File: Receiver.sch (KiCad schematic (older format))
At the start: 25 parts, among them U1 TL074

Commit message: Add files via upload
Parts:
- removed 1M1: R, Resistors_SMD:R_0603, symbol R
- added R?: 1K, Resistors_SMD:R_0603, symbol device:R
- C1, C3, C4, C5, C6, C7, C8: symbol C_Small -> device:C_Small
- C2: symbol CP1_Small -> device:CP1_Small
- D1: symbol BPW34 -> Receiver-rescue:BPW34-opto
- D2: symbol D -> device:D
- R1, R10, R11, R2, R3, R4, R5, R6, R7, R8, R9: symbol R -> device:R
- RV1, RV2: symbol POT -> Receiver-rescue:POT-device
- U1: symbol TL074 -> Receiver-rescue:TL074-linear
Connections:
- wire segments 65 -> 84
- no-connect marks 0 -> 2

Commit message: Add files via upload
Netzliste erstellt und Anfang von Layout
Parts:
- removed C2: CP1_Small, symbol device:CP1_Small
- added C2: 1u 50V, Capacitor_SMD:C_0603_1608Metric, symbol device:C_Small
- C1, C3, C4, C5, C6, C7, C8: footprint Capacitors_SMD:C_0603 -> Capacitor_SMD:C_0603_1608Metric
- D1: footprint Opto-Devices:PhotoDiode_DIL2_4.3x4.65_RM5.08 -> OptoDevice:Osram_DIL2_4.3x4.65mm_P5.08mm
- R1, R10, R2, R3, R4, R5, R6, R7, R8, R9: footprint Resistors_SMD:R_0603 -> Resistor_SMD:R_0603_1608Metric
- R11: renamed from R?; footprint Resistors_SMD:R_0603 -> Resistor_SMD:R_0603_1608Metric
- R12: renamed from R11; footprint Resistors_SMD:R_0603 -> Resistor_SMD:R_0603_1608Metric
- RV1, RV2: footprint (none) -> SparkFun-Electromechanical:TRIM_POT
- U1: value TL074 -> TL074 (ggf. durch TLV4172IPWR ersetzen); footprint Housings_SSOP:TSSOP-14_4.4x5mm_Pitch0.65mm -> Package_SO:TSSOP-14_4.4x5mm_P0.65mm

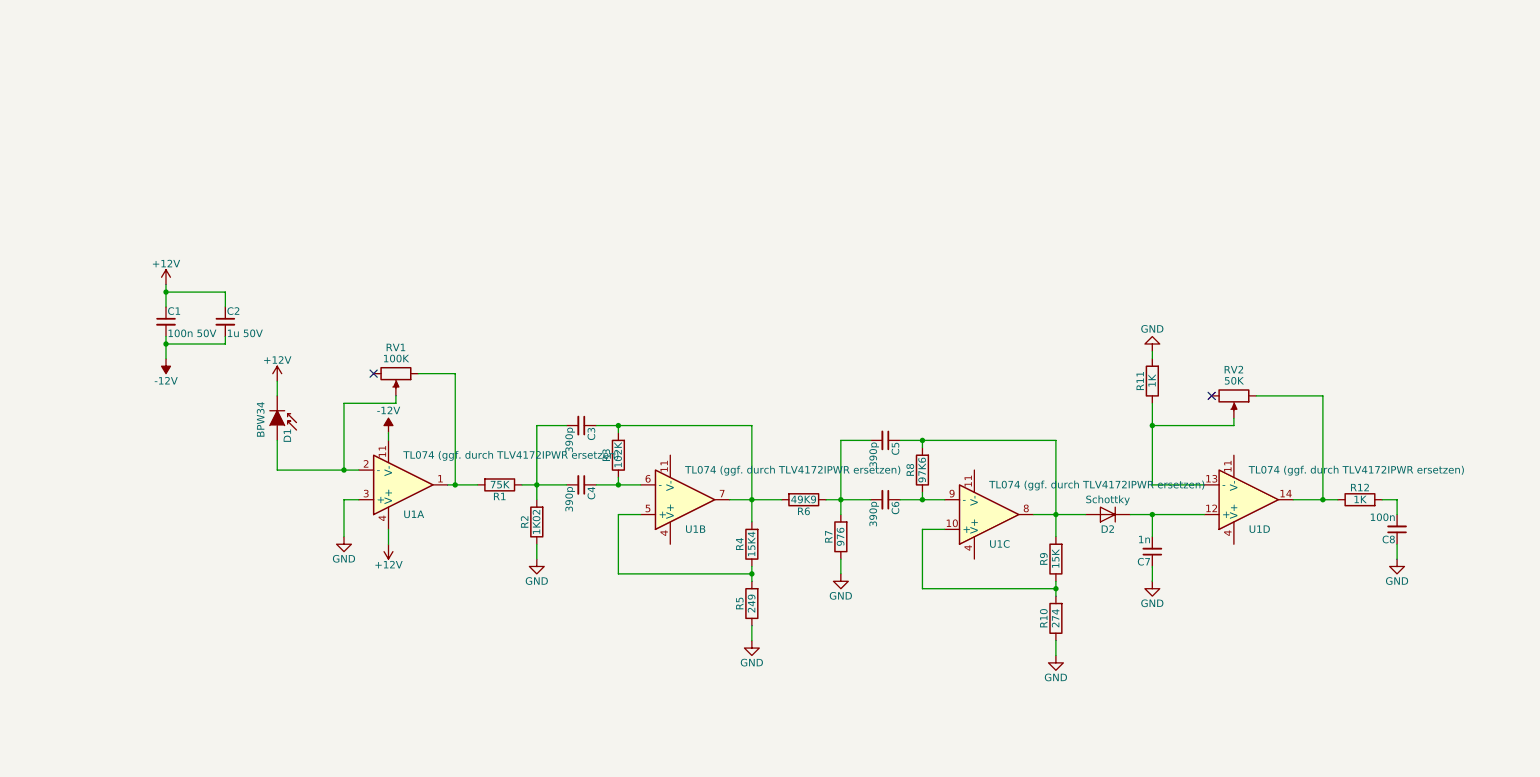
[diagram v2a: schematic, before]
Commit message: Add MST 201 banana plug to the library
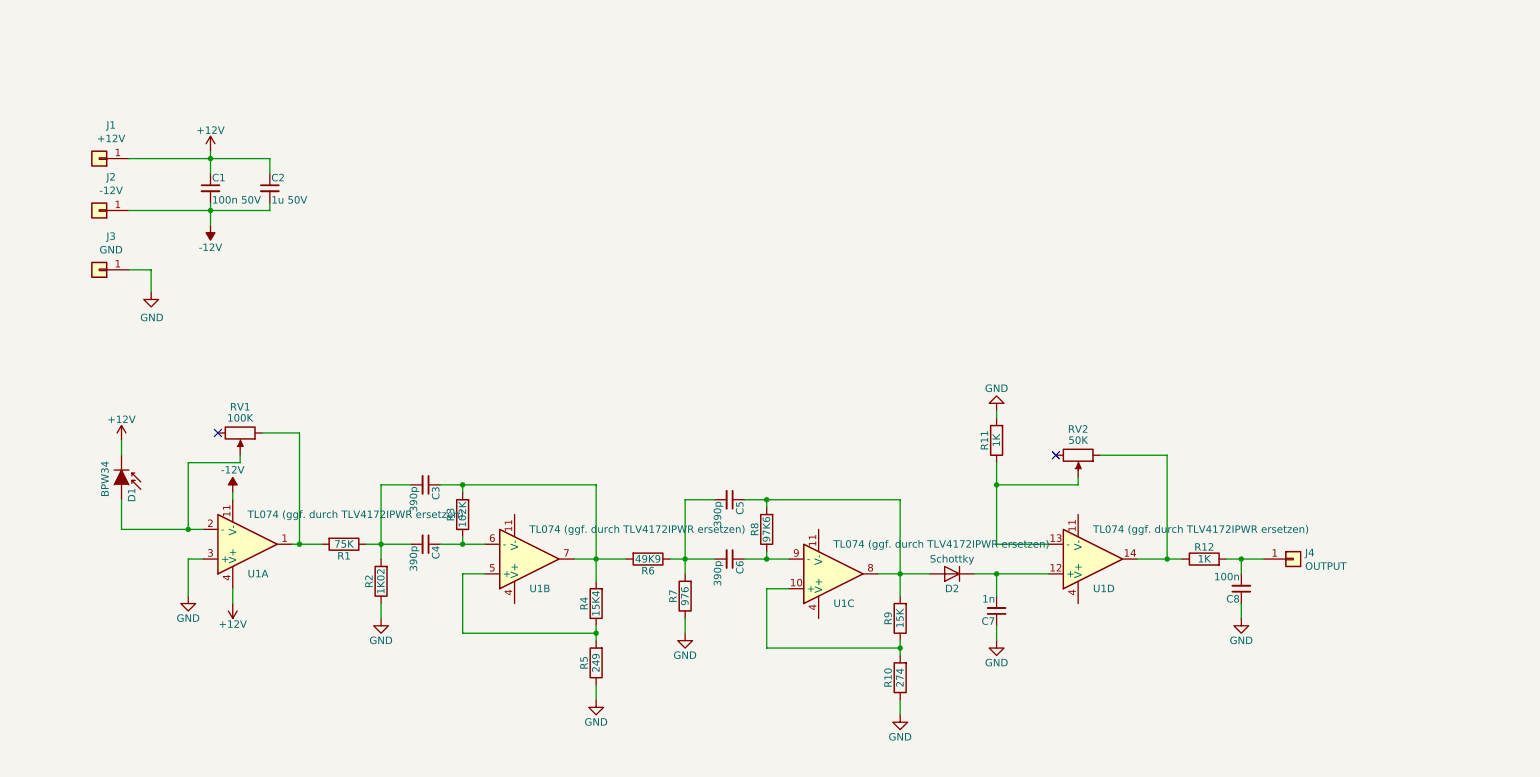
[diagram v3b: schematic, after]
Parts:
- added J1: +12V, optoreceiver:Hirschmann_MST201, symbol Connector:Conn_01x01
- added J2: -12V, optoreceiver:Hirschmann_MST201, symbol Connector:Conn_01x01
- added J3: GND, optoreceiver:Hirschmann_MST201, symbol Connector:Conn_01x01
- added J4: OUTPUT, optoreceiver:Hirschmann_MST201, symbol Connector:Conn_01x01
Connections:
- net +12V: now also J1.1 (Pin_1)
- net -12V: now also J2.1 (Pin_1)
- net GND: now also J3.1 (Pin_1)
- net at C8.2, R12.2: now also J4.1 (Pin_1)
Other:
- moved on the sheet: C1, C2, C3, C4, C5, C6, C7, C8, D1, D2, R1, R10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

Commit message: Update schematic and pcb
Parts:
- added D3, D4: LED, LEDs:LED_0603, symbol device:LED
- added J5: Conn_01x04, Pin_Headers:Pin_Header_Straight_1x04_Pitch2.54mm, symbol Connector:Conn_01x04
- added R13, R14: 1k, Resistors_SMD:R_0603, symbol device:R
- D2: value Schottky -> BAT54; footprint Diodes_SMD:D_SOD-123 -> Diodes_SMD:D_SOT-23_ANK
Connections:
- net +12V: now also J5.2 (Pin_2), R13.1
- net -12V: now also J5.3 (Pin_3), R14.1
- net GND: now also D3.1 (K), D4.2 (A), J5.4 (Pin_4)
- net OUTPUT: now reaches C8.2, J4.1 (Pin_1), R12.2
- net OUTPUT: now also J5.1 (Pin_1)
- new net: D3.2 (A), R13.2
- new net: D4.1 (K), R14.2
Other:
- moved on the sheet: J4
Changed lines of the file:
@@
 P 7700 4300
 F 0 "D2" H 7700 4400 50  0000 C CNN
-F 1 "Schottky " H 7700 4200 50  0000 C CNN
-F 2 "Diodes_SMD:D_SOD-123" H 7700 4300 50  0001 C CNN
+F 1 "BAT54" H 7700 4200 50  0000 C CNN
+F 2 "Diodes_SMD:D_SOT-23_ANK" H 7700 4300 50  0001 C CNN
 F 3 "" H 7700 4300 50  0001 C CNN
 	1    7700 4300
@@
 L Connector:Conn_01x01 J4
 U 1 1 5B03236E
-P 10000 4200
-F 0 "J4" H 10080 4242 50  0000 L CNN
-F 1 "OUTPUT" H 10080 4151 50  0000 L CNN
-F 2 "optoreceiver:Hirschmann_MST201" H 10000 4200 50  0001 C CNN
-F 3 "~" H 10000 4200 50  0001 C CNN
-	1    10000 4200
-	1    0    0    -1
+P 1950 1100
+F 0 "J4" H 2030 1142 50  0000 L CNN
+F 1 "OUTPUT" H 2030 1051 50  0000 L CNN
+F 2 "optoreceiver:Hirschmann_MST201" H 1950 1100 50  0001 C CNN
+F 3 "~" H 1950 1100 50  0001 C CNN
+	1    1950 1100
+	-1   0    0    1
 $EndComp
 Wire Wire Line
@@
 Wire Wire Line
 	2300 2250 2300 2400
+$Comp
+L device:LED D3
+U 1 1 5B14466C
+P 4300 2050
+F 0 "D3" V 4338 1933 50  0000 R CNN
+F 1 "LED" V 4247 1933 50  0000 R CNN
+F 2 "LEDs:LED_0603" H 4300 2050 50  0001 C CNN
+F 3 "~" H 4300 2050 50  0001 C CNN
+	1    4300 2050
+	0    -1   -1   0
+$EndComp
+Wire Wire Line
+	4300 2200 4300 2250
+$Comp
+L device:R R13
+U 1 1 5B14B3A1
+P 3700 1500
+F 0 "R13" H 3770 1546 50  0000 L CNN
+F 1 "1k" H 3770 1455 50  0000 L CNN
+F 2 "Resistors_SMD:R_0603" V 3630 1500 50  0001 C CNN
+F 3 "" H 3700 1500 50  0001 C CNN
+	1    3700 1500
+	0    -1   -1   0
+$EndComp
+$Comp
+L Connector:Conn_01x04 J5
+U 1 1 5B150E6D
+P 4850 1750
+F 0 "J5" H 4770 2067 50  0000 C CNN
+F 1 "Conn_01x04" H 4770 1976 50  0000 C CNN
+F 2 "Pin_Headers:Pin_Header_Straight_1x04_Pitch2.54mm" H 4850 1750 50  0001 C CNN
+F 3 "~" H 4850 1750 50  0001 C CNN
+	1    4850 1750
+	-1   0    0    -1
+$EndComp
+Text Label 2250 1100 0    50   ~ 0
+OUTPUT
+Wire Wire Line
+	2250 1100 2150 1100
+Text Label 9800 4200 0    50   ~ 0
+OUTPUT
+$Comp
+L power:GND #PWR0101
+U 1 1 5B156865
+P 5100 2000
+F 0 "#PWR0101" H 5100 1750 50  0001 C CNN
+F 1 "GND" H 5105 1827 50  0000 C CNN
+F 2 "" H 5100 2000 50  0001 C CNN
+F 3 "" H 5100 2000 50  0001 C CNN
+	1    5100 2000
+	1    0    0    -1
+$EndComp
+Wire Wire Line
+	5050 1950 5100 1950
+Wire Wire Line
+	5100 1950 5100 2000
+$Comp
+L power:+12V #PWR0102
+U 1 1 5B15914A
+P 5150 1750
+F 0 "#PWR0102" H 5150 1600 50  0001 C CNN
+F 1 "+12V" V 5165 1878 50  0000 L CNN
+F 2 "" H 5150 1750 50  0001 C CNN
+F 3 "" H 5150 1750 50  0001 C CNN
+	1    5150 1750
+	0    1    1    0
+$EndComp
+$Comp
+L power:-12V #PWR15
+U 1 1 5B15948E
+P 5150 1850
+F 0 "#PWR15" H 5150 1950 50  0001 C CNN
+F 1 "-12V" V 5165 1978 50  0000 L CNN
+F 2 "" H 5150 1850 50  0001 C CNN
+F 3 "" H 5150 1850 50  0001 C CNN
+	1    5150 1850
+	0    1    1    0
+$EndComp
+Wire Wire Line
+	5150 1850 5050 1850
+Wire Wire Line
+	5150 1750 5050 1750
+Text Label 5150 1650 0    50   ~ 0
+OUTPUT
+Wire Wire Line
+	5150 1650 5050 1650
+Wire Wire Line
+	3100 1500 3550 1500
+Connection ~ 3100 1500
+Wire Wire Line
+	2300 2250 4100 2250
+Connection ~ 2300 2250
+$Comp
+L device:R R14
+U 1 1 5B17749B
+P 3700 1850
+F 0 "R14" H 3770 1896 50  0000 L CNN
+F 1 "1k" H 3770 1805 50  0000 L CNN
+F 2 "Resistors_SMD:R_0603" V 3630 1850 50  0001 C CNN
+F 3 "" H 3700 1850 50  0001 C CNN
+	1    3700 1850
+	0    -1   -1   0
+$EndComp
+Wire Wire Line
+	3550 1850 3100 1850
+Connection ~ 3100 1850
+$Comp
+L device:LED D4
+U 1 1 5B182712
+P 4100 2050
+F 0 "D4" V 4138 1933 50  0000 R CNN
+F 1 "LED" V 4047 1933 50  0000 R CNN
+F 2 "LEDs:LED_0603" H 4100 2050 50  0001 C CNN
+F 3 "~" H 4100 2050 50  0001 C CNN
+	1    4100 2050
+	0    1    1    0
+$EndComp
+Wire Wire Line
+	4100 2200 4100 2250
+Connection ~ 4100 2250
+Wire Wire Line
+	4100 2250 4300 2250
+Wire Wire Line
+	3850 1850 4100 1850
+Wire Wire Line
+	4100 1850 4100 1900
+Wire Wire Line
+	3850 1500 4300 1500
+Wire Wire Line
+	4300 1500 4300 1900
 $EndSCHEMATC

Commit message: Add files via upload
- Platzierung und Silkscreen angepasst
- 3D Modelle ergänzt
- aktuelle Renderbilder erzeugt
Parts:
- C1, C2, C3, C4, C5, C6, C7, C8: symbol device:C_Small -> Device:C_Small
- D2: symbol device:D -> Device:D
- D3, D4: symbol device:LED -> Device:LED
- J1, J2, J3, J4: symbol Connector:Conn_01x01 -> Connector:Conn_01x01_Female
- J5: symbol Connector:Conn_01x04 -> Connector:Conn_01x04_Female
- R1, R10, R11, R12, R13, R14, R2, R3, R4, R5, R6, R7, R8, R9: symbol device:R -> Device:R
- RV1, RV2: footprint SparkFun-Electromechanical:TRIM_POT -> User-Submitted:BOURNS-3362P_pot
- U1: footprint Package_SO:TSSOP-14_4.4x5mm_P0.65mm -> Package_SO:SOIC-14_3.9x8.7mm_P1.27mm
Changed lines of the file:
@@
 F 0 "U1" H 2950 4300 50  0000 L CNN
 F 1 "TL074 (ggf. durch TLV4172IPWR ersetzen)" H 2950 3900 50  0000 L CNN
-F 2 "Package_SO:TSSOP-14_4.4x5mm_P0.65mm" H 2900 4200 50  0001 C CNN
+F 2 "Package_SO:SOIC-14_3.9x8.7mm_P1.27mm" H 2900 4200 50  0001 C CNN
 F 3 "" H 3000 4300 50  0001 C CNN
 	1    2950 4100
@@
 $EndComp
 $Comp
-L power:-12V #PWR5
+L power:-12V #PWR05
 U 1 1 5AEAF2F4
 P 2850 3750
-F 0 "#PWR5" H 2850 3850 50  0001 C CNN
+F 0 "#PWR05" H 2850 3850 50  0001 C CNN
 F 1 "-12V" H 2850 3900 50  0000 C CNN
 F 2 "" H 2850 3750 50  0001 C CNN
@@
 	1    0    0    -1
 $EndComp
-Wire Wire Line
-	2850 4400 2850 4500
-Wire Wire Line
-	2850 3750 2850 3800
 Wire Wire Line
 	2550 4000 2650 4000
@@
 F 0 "U1" H 4850 4400 50  0000 L CNN
 F 1 "TL074 (ggf. durch TLV4172IPWR ersetzen)" H 4850 4000 50  0000 L CNN
-F 2 "Package_SO:TSSOP-14_4.4x5mm_P0.65mm" H 4800 4300 50  0001 C CNN
+F 2 "Package_SO:SOIC-14_3.9x8.7mm_P1.27mm" H 4800 4300 50  0001 C CNN
 F 3 "" H 4900 4400 50  0001 C CNN
 	2    4850 4200
@@
 $EndComp
 $Comp
-L device:R R1
+L Device:R R1
 U 1 1 5AEAF541
 P 3600 4100
@@
 $EndComp
 $Comp
-L device:R R2
+L Device:R R2
 U 1 1 5AEAF581
 P 3850 4350
@@
 	3850 3700 3850 4100
 $Comp
-L device:C_Small C4
+L Device:C_Small C4
 U 1 1 5AEAF686
 P 4150 4100
@@
 $EndComp
 $Comp
-L device:C_Small C3
+L Device:C_Small C3
 U 1 1 5AEAF715
 P 4150 3700
@@
 	4250 4100 4400 4100
 $Comp
-L device:R R3
+L Device:R R3
 U 1 1 5AEAF96B
 P 4400 3900
@@
 Connection ~ 4400 3700
 $Comp
-L device:R R4
+L Device:R R4
 U 1 1 5AEAFA8E
 P 5300 4500
@@
 $EndComp
 $Comp
-L device:R R5
+L Device:R R5
 U 1 1 5AEAFAD7
 P 5300 4900
@@
 F 0 "U1" H 6900 4500 50  0000 L CNN
 F 1 "TL074 (ggf. durch TLV4172IPWR ersetzen)" H 6900 4100 50  0000 L CNN
-F 2 "Package_SO:TSSOP-14_4.4x5mm_P0.65mm" H 6850 4400 50  0001 C CNN
+F 2 "Package_SO:SOIC-14_3.9x8.7mm_P1.27mm" H 6850 4400 50  0001 C CNN
 F 3 "" H 6950 4500 50  0001 C CNN
 	3    6900 4300
@@
 $EndComp
 $Comp
-L device:R R6
+L Device:R R6
 U 1 1 5AEAFDA7
 P 5650 4200
@@
 $EndComp
 $Comp
-L device:R R7
+L Device:R R7
 U 1 1 5AEAFDAD
 P 5900 4450
@@
 	5900 3800 5900 4200
 $Comp
-L device:C_Small C6
+L Device:C_Small C6
 U 1 1 5AEAFDBC
 P 6200 4200
@@
 $EndComp
 $Comp
-L device:C_Small C5
+L Device:C_Small C5
 U 1 1 5AEAFDC2
 P 6200 3800
@@
 	6300 4200 6450 4200
 $Comp
-L device:R R8
+L Device:R R8
 U 1 1 5AEAFDC9
 P 6450 4000
@@
 Connection ~ 6450 3800
 $Comp
-L device:R R9
+L Device:R R9
 U 1 1 5AEAFDD8
 P 7350 4600
@@
 $EndComp
 $Comp
-L device:R R10
+L Device:R R10
 U 1 1 5AEAFDDE
 P 7350 5000
@@
 	7350 5150 7350 5250
 $Comp
-L device:C_Small C1
+L Device:C_Small C1
 U 1 1 5AEAFE56
 P 2700 1700
@@
 	2700 1450 2700 1500
 $Comp
-L power:-12V #PWR2
+L power:-12V #PWR02
 U 1 1 5AEAFF86
 P 2700 1950
-F 0 "#PWR2" H 2700 2050 50  0001 C CNN
+F 0 "#PWR02" H 2700 2050 50  0001 C CNN
 F 1 "-12V" H 2700 2100 50  0000 C CNN
 F 2 "" H 2700 1950 50  0001 C CNN
@@
 F 0 "RV2" V 8375 3500 50  0000 C CNN
 F 1 "50K" V 8450 3500 50  0000 C CNN
-F 2 "SparkFun-Electromechanical:TRIM_POT" H 8550 3500 50  0001 C CNN
+F 2 "User-Submitted:BOURNS-3362P_pot" H 8550 3500 50  0001 C CNN
 F 3 "" H 8550 3500 50  0001 C CNN
 	1    8550 3500
@@
 $EndComp
 $Comp
-L device:D D2
+L Device:D D2
 U 1 1 5AEB05C3
 P 7700 4300
@@
 $EndComp
 $Comp
-L device:C_Small C7
+L Device:C_Small C7
 U 1 1 5AEB0668
 P 8000 4550
@@
 Wire Wire Line
 	7850 4300 8000 4300
-$Comp
-L Receiver-rescue:TL074-linear U1
-U 4 1 5AEB085F
-P 8650 4200
-F 0 "U1" H 8650 4400 50  0000 L CNN
-F 1 "TL074 (ggf. durch TLV4172IPWR ersetzen)" H 8650 4000 50  0000 L CNN
-F 2 "Package_SO:TSSOP-14_4.4x5mm_P0.65mm" H 8600 4300 50  0001 C CNN
-F 3 "" H 8700 4400 50  0001 C CNN
-	4    8650 4200
-	1    0    0    1
-$EndComp
 Connection ~ 8000 4300
 Wire Wire Line
@@
 	8950 4200 9150 4200
 $Comp
-L device:R R12
+L Device:R R12
 U 1 1 5AEB0CD1
 P 9400 4200
@@
 Connection ~ 9150 4200
 $Comp
-L device:C_Small C8
+L Device:C_Small C8
 U 1 1 5AEB0DB0
 P 9650 4400
@@
 F 0 "RV1" V 2725 3350 50  0000 C CNN
 F 1 "100K" V 2800 3350 50  0000 C CNN
-F 2 "SparkFun-Electromechanical:TRIM_POT" H 2900 3350 50  0001 C CNN
+F 2 "User-Submitted:BOURNS-3362P_pot" H 2900 3350 50  0001 C CNN
 F 3 "" H 2900 3350 50  0001 C CNN
 	1    2900 3350
@@
 	2100 4000 2550 4000
 $Comp
-L device:R R11
+L Device:R R11
 U 1 1 5AF96B45
 P 8000 3400
@@
 NoConn ~ 8400 3500
 $Comp
-L device:C_Small C2
+L Device:C_Small C2
 U 1 1 5AFB3597
 P 3100 1700
@@
 $EndComp
 $Comp
-L Connector:Conn_01x01 J1
+L Connector:Conn_01x01_Female J1
 U 1 1 5B031E2F
 P 1950 1500
@@
 $EndComp
 $Comp
-L Connector:Conn_01x01 J3
+L Connector:Conn_01x01_Female J3
 U 1 1 5B0321C2
 P 1950 2250
@@
 $EndComp
 $Comp
-L Connector:Conn_01x01 J2
+L Connector:Conn_01x01_Female J2
 U 1 1 5B032258
 P 1950 1850
@@
 $EndComp
 $Comp
-L Connector:Conn_01x01 J4
+L Connector:Conn_01x01_Female J4
 U 1 1 5B03236E
 P 1950 1100
@@
 	2300 2250 2300 2400
 $Comp
-L device:LED D3
+L Device:LED D3
 U 1 1 5B14466C
 P 4300 2050
@@
 	4300 2200 4300 2250
 $Comp
-L device:R R13
+L Device:R R13
 U 1 1 5B14B3A1
 P 3700 1500
@@
 $EndComp
 $Comp
-L Connector:Conn_01x04 J5
+L Connector:Conn_01x04_Female J5
 U 1 1 5B150E6D
 P 4850 1750
@@
 $EndComp
 $Comp
-L power:-12V #PWR15
+L power:-12V #PWR015
 U 1 1 5B15948E
 P 5150 1850
-F 0 "#PWR15" H 5150 1950 50  0001 C CNN
+F 0 "#PWR015" H 5150 1950 50  0001 C CNN
 F 1 "-12V" V 5165 1978 50  0000 L CNN
 F 2 "" H 5150 1850 50  0001 C CNN
@@
 Connection ~ 2300 2250
 $Comp
-L device:R R14
+L Device:R R14
 U 1 1 5B17749B
 P 3700 1850
@@
 Connection ~ 3100 1850
 $Comp
-L device:LED D4
+L Device:LED D4
 U 1 1 5B182712
 P 4100 2050
@@
 Wire Wire Line
 	4300 1500 4300 1900
+Wire Wire Line
+	2850 4400 2850 4500
+Wire Wire Line
+	2850 3750 2850 3800
+$Comp
+L power:+12V #PWR0104
+U 1 1 5B16DE44
+P 4750 4500
+F 0 "#PWR0104" H 4750 4350 50  0001 C CNN
+F 1 "+12V" H 4750 4640 50  0000 C CNN
+F 2 "" H 4750 4500 50  0001 C CNN
+F 3 "" H 4750 4500 50  0001 C CNN
+	1    4750 4500
+	-1   0    0    1
+$EndComp
+$Comp
+L Receiver-rescue:TL074-linear U1
+U 4 1 5AEB085F
+P 8650 4200
+F 0 "U1" H 8650 4400 50  0000 L CNN
+F 1 "TL074 (ggf. durch TLV4172IPWR ersetzen)" H 8650 4000 50  0000 L CNN
+F 2 "Package_SO:SOIC-14_3.9x8.7mm_P1.27mm" H 8600 4300 50  0001 C CNN
+F 3 "" H 8700 4400 50  0001 C CNN
+	4    8650 4200
+	1    0    0    1
+$EndComp
 $EndSCHEMATC

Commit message: Real Value Simulation + Update in Schematic
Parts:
- C3, C4: value 390p -> 750p
- C5, C6: value 390p -> 820p
- R1: value 75K -> 24K
- R10: value 274 -> 360
- R2: value 1K02 -> 1K
- R3: value 102K -> 100K
- R4: value 15K4 -> 22K
- R5: value 249 -> 360
- R6: value 49K9 -> 24K
- R7: value 976 -> 1K
- R8: value 97K6 -> 100K
- R9: value 15K -> 22K
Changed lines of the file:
@@
 P 3600 4100
 F 0 "R1" V 3680 4100 50  0000 C CNN
-F 1 "75K" V 3600 4100 50  0000 C CNN
+F 1 "24K" V 3600 4100 50  0000 C CNN
 F 2 "Resistor_SMD:R_0603_1608Metric" V 3530 4100 50  0001 C CNN
 F 3 "" H 3600 4100 50  0001 C CNN
@@
 P 3850 4350
 F 0 "R2" V 3930 4350 50  0000 C CNN
-F 1 "1K02" V 3850 4350 50  0000 C CNN
+F 1 "1K" V 3850 4350 50  0000 C CNN
 F 2 "Resistor_SMD:R_0603_1608Metric" V 3780 4350 50  0001 C CNN
 F 3 "" H 3850 4350 50  0001 C CNN
@@
 P 4150 4100
 F 0 "C4" H 4160 4170 50  0000 L CNN
-F 1 "390p" H 4160 4020 50  0000 L CNN
+F 1 "750p" H 4160 4020 50  0000 L CNN
 F 2 "Capacitor_SMD:C_0603_1608Metric" H 4150 4100 50  0001 C CNN
 F 3 "" H 4150 4100 50  0001 C CNN
@@
 P 4150 3700
 F 0 "C3" H 4160 3770 50  0000 L CNN
-F 1 "390p" H 4160 3620 50  0000 L CNN
+F 1 "750p" H 4160 3620 50  0000 L CNN
 F 2 "Capacitor_SMD:C_0603_1608Metric" H 4150 3700 50  0001 C CNN
 F 3 "" H 4150 3700 50  0001 C CNN
@@
 P 4400 3900
 F 0 "R3" V 4480 3900 50  0000 C CNN
-F 1 "102K" V 4400 3900 50  0000 C CNN
+F 1 "100K" V 4400 3900 50  0000 C CNN
 F 2 "Resistor_SMD:R_0603_1608Metric" V 4330 3900 50  0001 C CNN
 F 3 "" H 4400 3900 50  0001 C CNN
@@
 P 5300 4500
 F 0 "R4" V 5380 4500 50  0000 C CNN
-F 1 "15K4" V 5300 4500 50  0000 C CNN
+F 1 "22K" V 5300 4500 50  0000 C CNN
 F 2 "Resistor_SMD:R_0603_1608Metric" V 5230 4500 50  0001 C CNN
 F 3 "" H 5300 4500 50  0001 C CNN
@@
 P 5300 4900
 F 0 "R5" V 5380 4900 50  0000 C CNN
-F 1 "249" V 5300 4900 50  0000 C CNN
+F 1 "360" V 5300 4900 50  0000 C CNN
 F 2 "Resistor_SMD:R_0603_1608Metric" V 5230 4900 50  0001 C CNN
 F 3 "" H 5300 4900 50  0001 C CNN
@@
 P 5650 4200
 F 0 "R6" V 5730 4200 50  0000 C CNN
-F 1 "49K9" V 5650 4200 50  0000 C CNN
+F 1 "24K" V 5650 4200 50  0000 C CNN
 F 2 "Resistor_SMD:R_0603_1608Metric" V 5580 4200 50  0001 C CNN
 F 3 "" H 5650 4200 50  0001 C CNN
@@
 P 5900 4450
 F 0 "R7" V 5980 4450 50  0000 C CNN
-F 1 "976" V 5900 4450 50  0000 C CNN
+F 1 "1K" V 5900 4450 50  0000 C CNN
 F 2 "Resistor_SMD:R_0603_1608Metric" V 5830 4450 50  0001 C CNN
 F 3 "" H 5900 4450 50  0001 C CNN
@@
 P 6200 4200
 F 0 "C6" H 6210 4270 50  0000 L CNN
-F 1 "390p" H 6210 4120 50  0000 L CNN
+F 1 "820p" H 6210 4120 50  0000 L CNN
 F 2 "Capacitor_SMD:C_0603_1608Metric" H 6200 4200 50  0001 C CNN
 F 3 "" H 6200 4200 50  0001 C CNN
@@
 P 6200 3800
 F 0 "C5" H 6210 3870 50  0000 L CNN
-F 1 "390p" H 6210 3720 50  0000 L CNN
+F 1 "820p" H 6210 3720 50  0000 L CNN
 F 2 "Capacitor_SMD:C_0603_1608Metric" H 6200 3800 50  0001 C CNN
 F 3 "" H 6200 3800 50  0001 C CNN
@@
 P 6450 4000
 F 0 "R8" V 6530 4000 50  0000 C CNN
-F 1 "97K6" V 6450 4000 50  0000 C CNN
+F 1 "100K" V 6450 4000 50  0000 C CNN
 F 2 "Resistor_SMD:R_0603_1608Metric" V 6380 4000 50  0001 C CNN
 F 3 "" H 6450 4000 50  0001 C CNN
@@
 P 7350 4600
 F 0 "R9" V 7430 4600 50  0000 C CNN
-F 1 "15K" V 7350 4600 50  0000 C CNN
+F 1 "22K" V 7350 4600 50  0000 C CNN
 F 2 "Resistor_SMD:R_0603_1608Metric" V 7280 4600 50  0001 C CNN
 F 3 "" H 7350 4600 50  0001 C CNN
@@
 P 7350 5000
 F 0 "R10" V 7430 5000 50  0000 C CNN
-F 1 "274" V 7350 5000 50  0000 C CNN
+F 1 "360" V 7350 5000 50  0000 C CNN
 F 2 "Resistor_SMD:R_0603_1608Metric" V 7280 5000 50  0001 C CNN
 F 3 "" H 7350 5000 50  0001 C CNN

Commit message: changed values in schematic
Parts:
- C8: value 100n -> 22u
- R11: value 1K -> 100R
- R13, R14: value 1k -> 2k
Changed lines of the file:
@@
 P 9650 4400
 F 0 "C8" H 9660 4470 50  0000 L CNN
-F 1 "100n" H 9660 4320 50  0000 L CNN
+F 1 "22u" H 9660 4320 50  0000 L CNN
 F 2 "Capacitor_SMD:C_0603_1608Metric" H 9650 4400 50  0001 C CNN
 F 3 "" H 9650 4400 50  0001 C CNN
@@
 P 8000 3400
 F 0 "R11" V 8080 3400 50  0000 C CNN
-F 1 "1K" V 8000 3400 50  0000 C CNN
+F 1 "100R" V 8000 3400 50  0000 C CNN
 F 2 "Resistor_SMD:R_0603_1608Metric" V 7930 3400 50  0001 C CNN
 F 3 "" H 8000 3400 50  0001 C CNN
@@
 P 3700 1500
 F 0 "R13" H 3770 1546 50  0000 L CNN
-F 1 "1k" H 3770 1455 50  0000 L CNN
+F 1 "2k" H 3770 1455 50  0000 L CNN
 F 2 "Resistors_SMD:R_0603" V 3630 1500 50  0001 C CNN
 F 3 "" H 3700 1500 50  0001 C CNN
@@
 P 3700 1850
 F 0 "R14" H 3770 1896 50  0000 L CNN
-F 1 "1k" H 3770 1805 50  0000 L CNN
+F 1 "2k" H 3770 1805 50  0000 L CNN
 F 2 "Resistors_SMD:R_0603" V 3630 1850 50  0001 C CNN
 F 3 "" H 3700 1850 50  0001 C CNN
